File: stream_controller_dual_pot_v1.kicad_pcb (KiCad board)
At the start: 2 copper layers, 46.5 x 48 mm, 39 parts, among them Q1 Q_PMOS_GDS, Q2 Q_PMOS_GDS, SW1 SW_SPDT, U1 MCP1825S, U2 MCP2221AxSL, U3 MCP73831-2-OT, U5 ESP32_WROVER_E, U6 MIC803

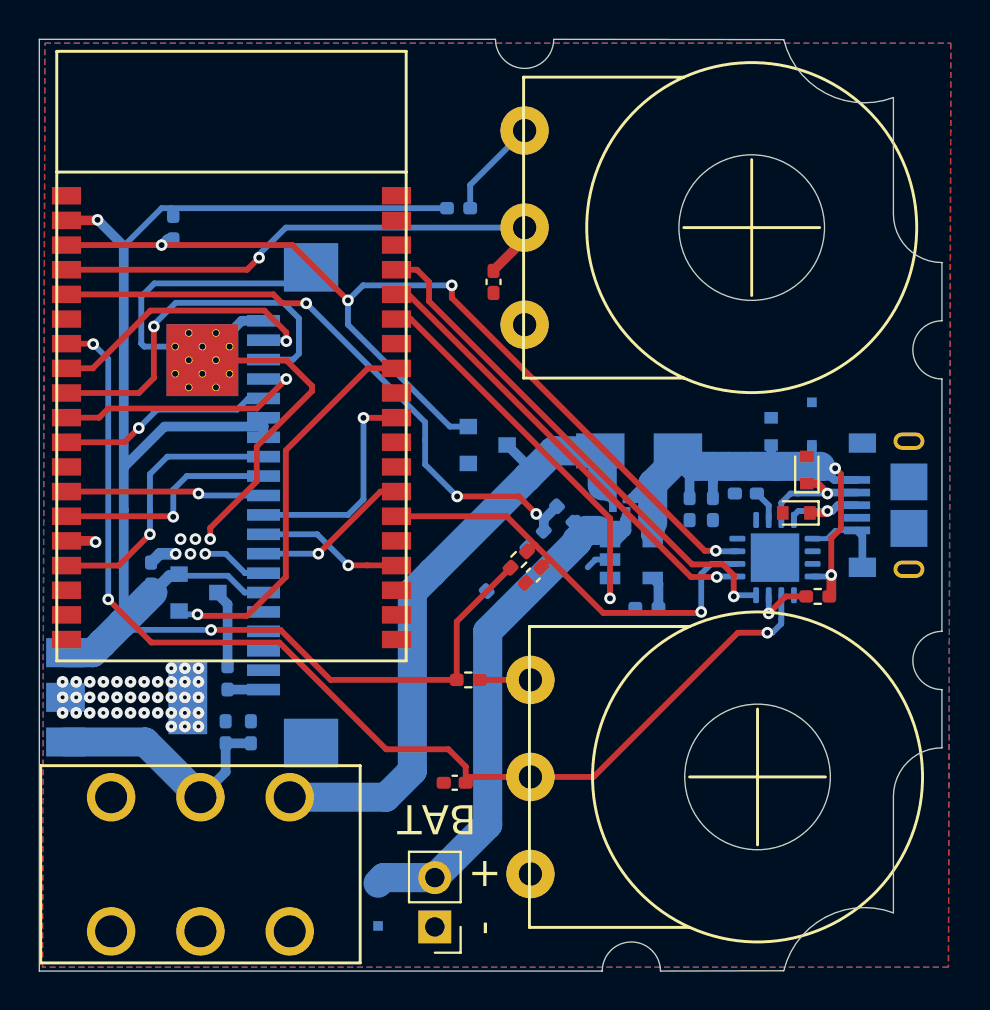
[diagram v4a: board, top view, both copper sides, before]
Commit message: Corrections et ajouts
Corrigé : strapping pin 2 connectée au même signal FLASH que pin 0
Ajouté : I2C entre uC et contrôleur USB
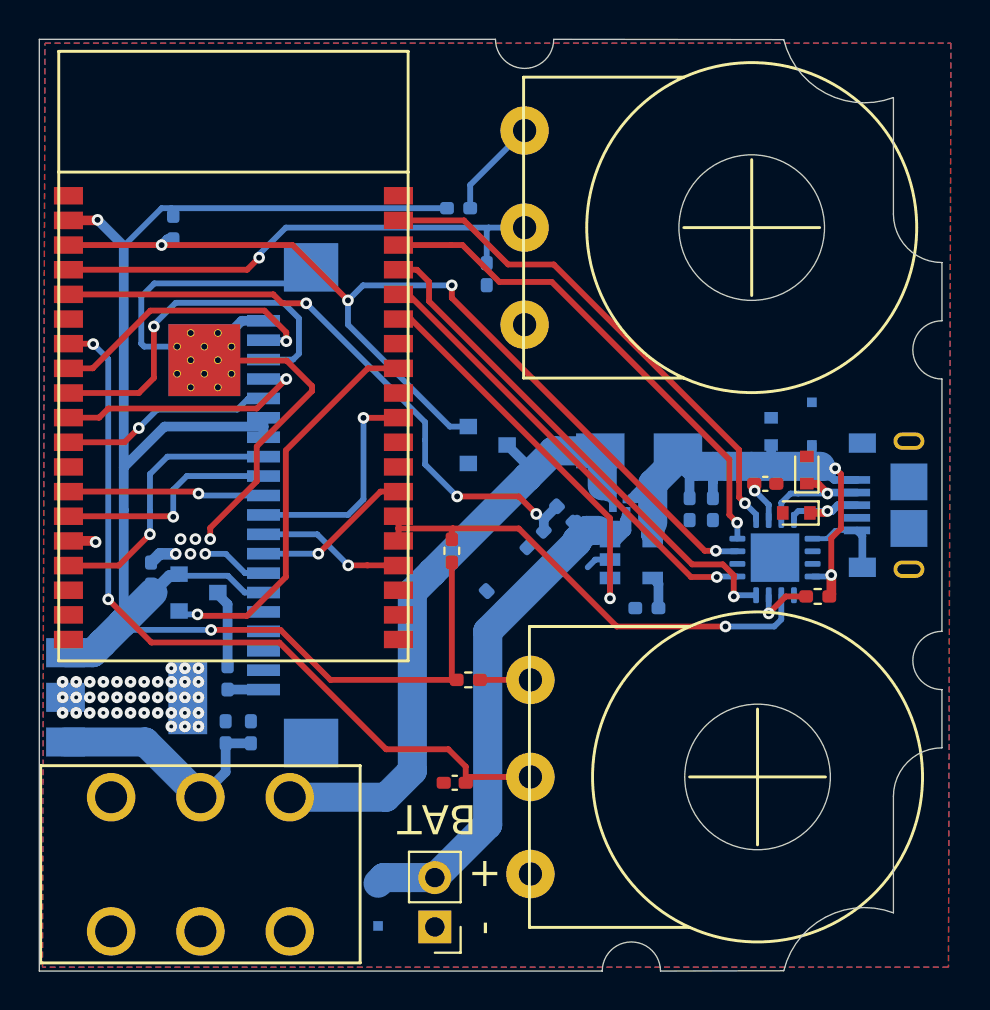
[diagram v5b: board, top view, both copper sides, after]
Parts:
- removed C10: 100nF 25V, Capacitor_SMD:C_0402_1005Metric_Pad0.74x0.62mm_HandSolder
- C2: moved to F.Cu
- C9: moved to B.Cu
- moved R8 3.48 mm to (63.8, 32.4), turned to 90 degrees
- moved C2 1.12 mm to (79.9, 28.9), turned to 180 degrees
- moved C9 0.53 mm to (65.5, 18.1)
- moved U5 0.10 mm to (52.5, 25.5)
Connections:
- U2 pad 2: POT2 -> FLASH
- U2 pad 6: FLASH -> (no net)
- U2 pad 8: (no net) -> I2C_SDA
- U2 pad 9: (no net) -> I2C_SCL
- U5 pad 24: (no net) -> FLASH
- U5 pad 36: (no net) -> I2C_SDA
- U5 pad 37: (no net) -> I2C_SCL
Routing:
- net I2C_SCL: track 0.00 -> 26.4 mm, vias 0 -> 1
- net I2C_SDA: track 0.00 -> 25.9 mm, vias 0 -> 1
- net POT2: track 58.8 -> 41.2 mm, vias 3 -> 2
- net FLASH: track 23.1 -> 25.1 mm
- net 3V3: track 92.9 -> 92.1 mm
- net POT1: track 27.6 -> 26.8 mm
- net Net-(C2-Pad2): track 1.61 -> 2.17 mm, vias 0 -> 1
